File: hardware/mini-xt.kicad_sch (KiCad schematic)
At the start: 0 parts

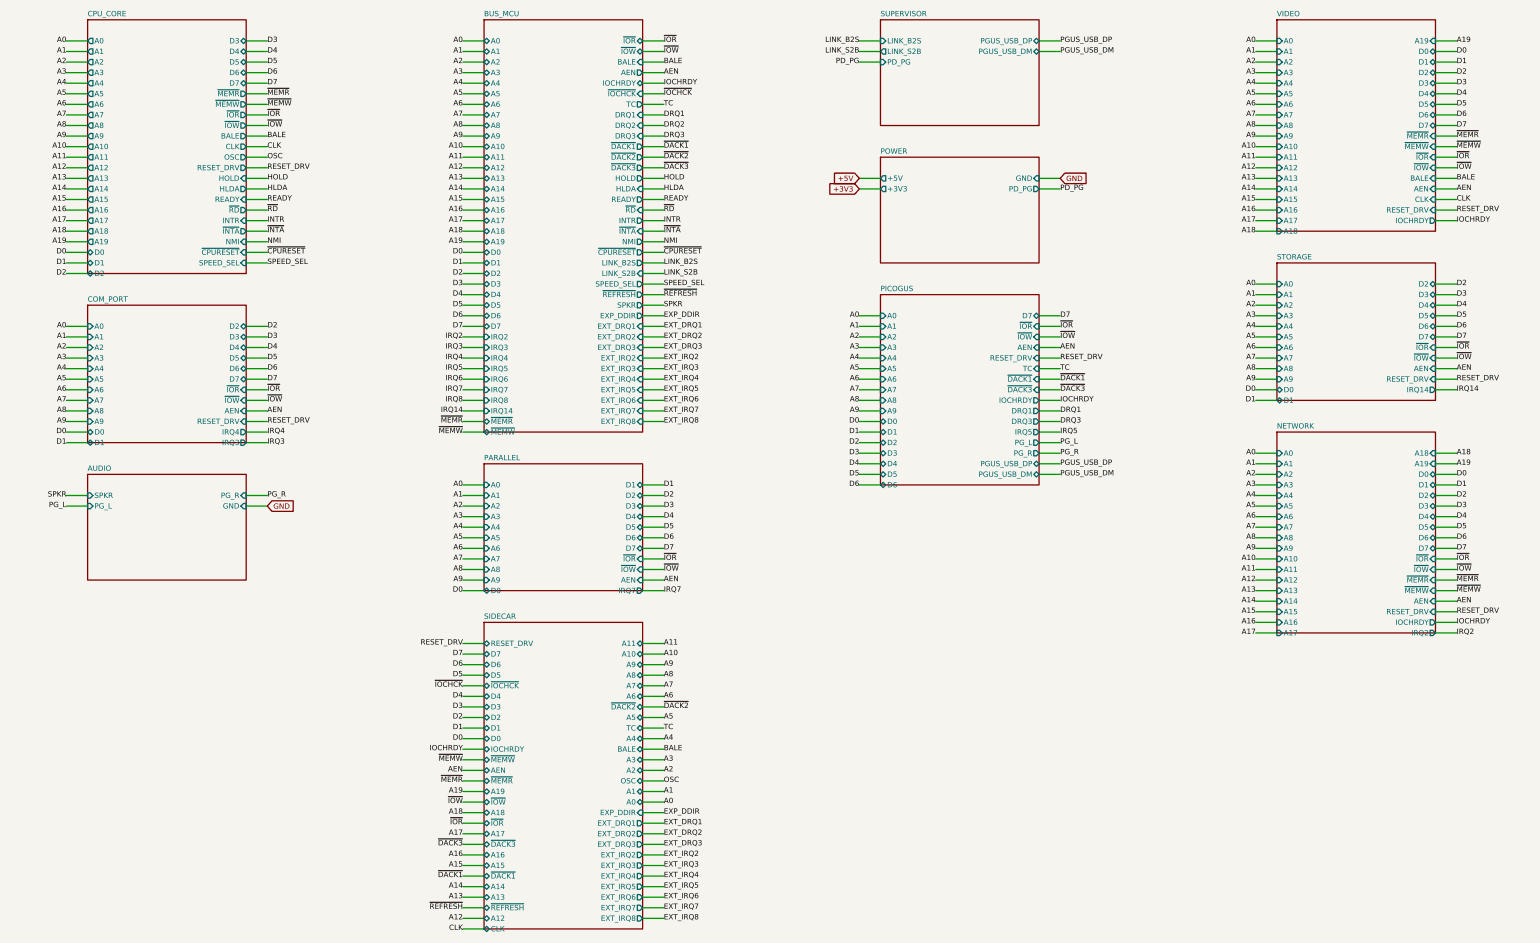
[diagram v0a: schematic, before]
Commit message: addr_decode: central I/O decode, IRQ mapping + disable jumpers; UART -> TL16C550CPFBR
New addr_decode sheet owns the discrete peripherals' bus plumbing:
'138+'00+'32 windowed decode exports ~COM1/~COM2/~LPT/~IDE chip selects
(0x3F8/0x2F8/0x378 share one A5.A4.A3 fine term); one shared 74LVC125A
maps the peripherals' private IRQ requests onto IRQ4/3/7/14 (COM keeps
~OUT2 gating), replacing the three per-sheet '125s; base straps (JP1/JP2,
pulled-high commons) and per-peripheral disable jumpers JP3-JP6 (enabled
by default, fit to disable via a second '32 rank on the CS) live here.
com_port/parallel/storage lose their decode gates, IRQ drivers and
enable jumpers; board drops 97 -> 93 ICs. Docs reframed per feedback:
PRIV_CS/PRIV_IRQREQ are shared logic factored out, not isolation breaks.

UART rebound to the active TL16C550CPFBR (TQFP-48, LCSC C882798, thin
stock) -- pinout verified identical to the symbol via jlc_get_pinout;
parts.py-only swap, sourcing notes updated.

Co-Authored-By: Claude Fable 5 <noreply@anthropic.com>
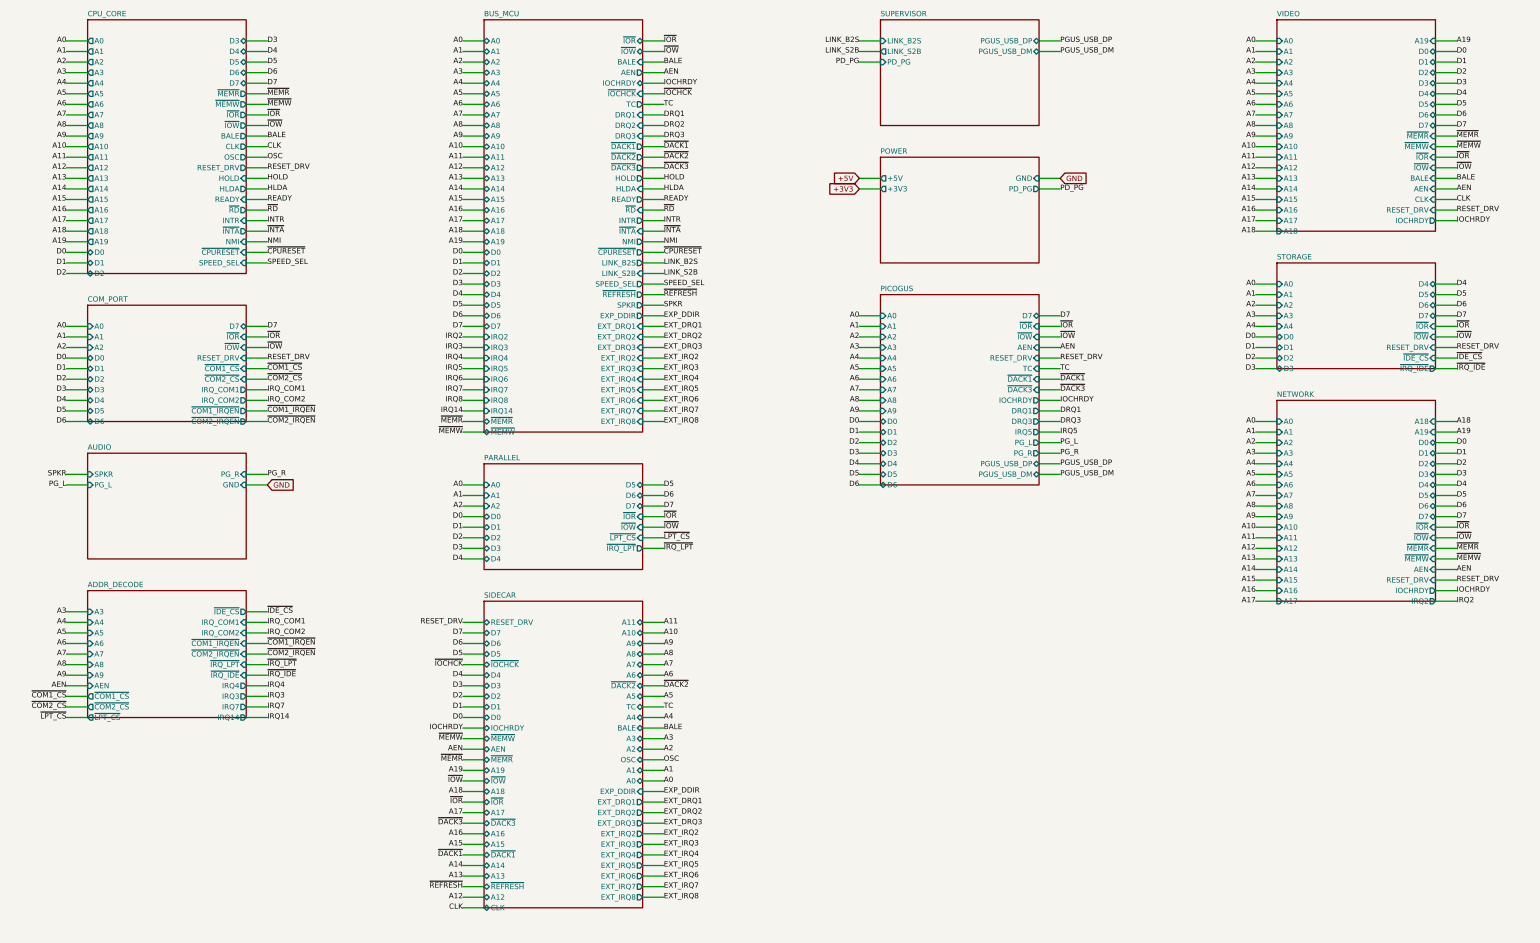
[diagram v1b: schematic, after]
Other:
- added sheet ADDR_DECODE (sheets/addr_decode.kicad_sch)
- sheet COM_PORT ports: added IRQ_COM1, IRQ_COM2, ~{COM1_CS}, ~{COM1_IRQEN}, ~{COM2_CS}, ~{COM2_IRQEN}; removed A3, A4, A5, A6, A7, A8, A9, AEN, IRQ3, IRQ4
- sheet PARALLEL ports: added ~{IRQ_LPT}, ~{LPT_CS}; removed A3, A4, A5, A6, A7, A8, A9, AEN, IRQ7
- sheet STORAGE ports: added ~{IDE_CS}, ~{IRQ_IDE}; removed A5, A6, A7, A8, A9, AEN, IRQ14

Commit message: addr_decode: hardwire LPT/IDE bases; centralize NIC + video disables (JP1-JP6)
LPT fixed at 0x378, IDE at 0x300 -- both base straps and their pull-ups
deleted ('138 ~Y1 now NC, the '00's ~A5 gate spare, IDE OR-leg takes raw
A5). The NIC and video disable jumpers move to addr_decode as JP5/JP6
with the same fit-to-disable sense as the rest: their gating hardware
stays local (the NIC's isolation '125 inside the 5V island, video's
firmware boot strap on GPIO42), only the jumper levels cross as
mxbus.PRIV_DIS -- video's documented firmware polarity inverts (high =
disabled; no firmware exists yet). Disable row is now a uniform JP1-JP6
(COM1/COM2/LPT/IDE/NIC/VID), bare board runs everything; network JP1/R6
and video JP1/R30 deleted, VID_BASE becomes video JP1. card_video's
wrapper re-adds a local DIS_VID strap (the documented PRIV lift
pattern). Docs/tables/decision logs aligned.

Co-Authored-By: Claude Fable 5 <noreply@anthropic.com>
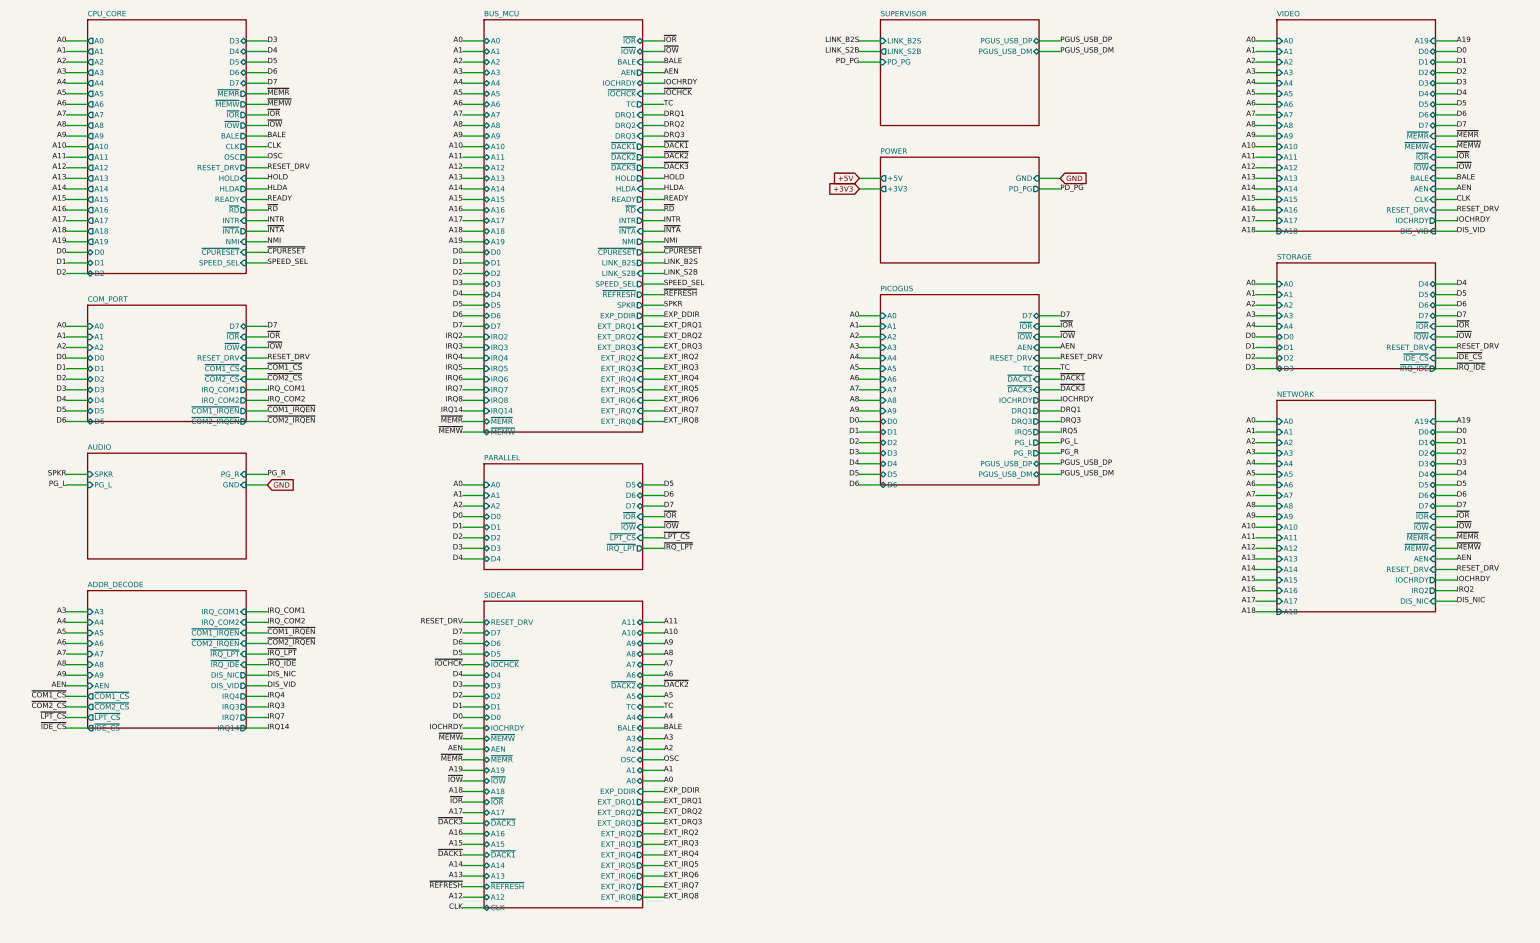
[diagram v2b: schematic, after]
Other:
- sheet ADDR_DECODE ports: added DIS_NIC, DIS_VID; removed none
- sheet NETWORK ports: added DIS_NIC; removed none
- sheet VIDEO ports: added DIS_VID; removed none

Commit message: bus_mcu: delete U17 (74LVC04A, 1/6 gates) -- HLDA inverter moves to parallel's spare gate
The HLDA -> ~{HLDA} inversion for the counter '244s now lives on the
parallel sheet's spare 74AHC14 Schmitt gate (U9.1, freed by the decode
centralization) -- the board's only spare 5V-tolerant inverter, which is
what HLDA (raw 5V V20 output) requires. ~{HLDA} joins mxbus.PRIV_CPU and
crosses as an interface net; park-safety unchanged (R18 parks HLDA low,
~{HLDA} idles high, '244s off during MCU-Hi-Z). U17 + its decoupler
deleted; the orphaned 74LVC04A parts.py line (C282341) removed. Board
454 comps / 92 ICs. Also sweeps stale JP-number refs left in the
parallel/storage/com_port docstrings from the jumper renumber.

Co-Authored-By: Claude Fable 5 <noreply@anthropic.com>
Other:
- sheet BUS_MCU ports: added ~{HLDA}; removed none
- sheet PARALLEL ports: added HLDA, ~{HLDA}; removed none

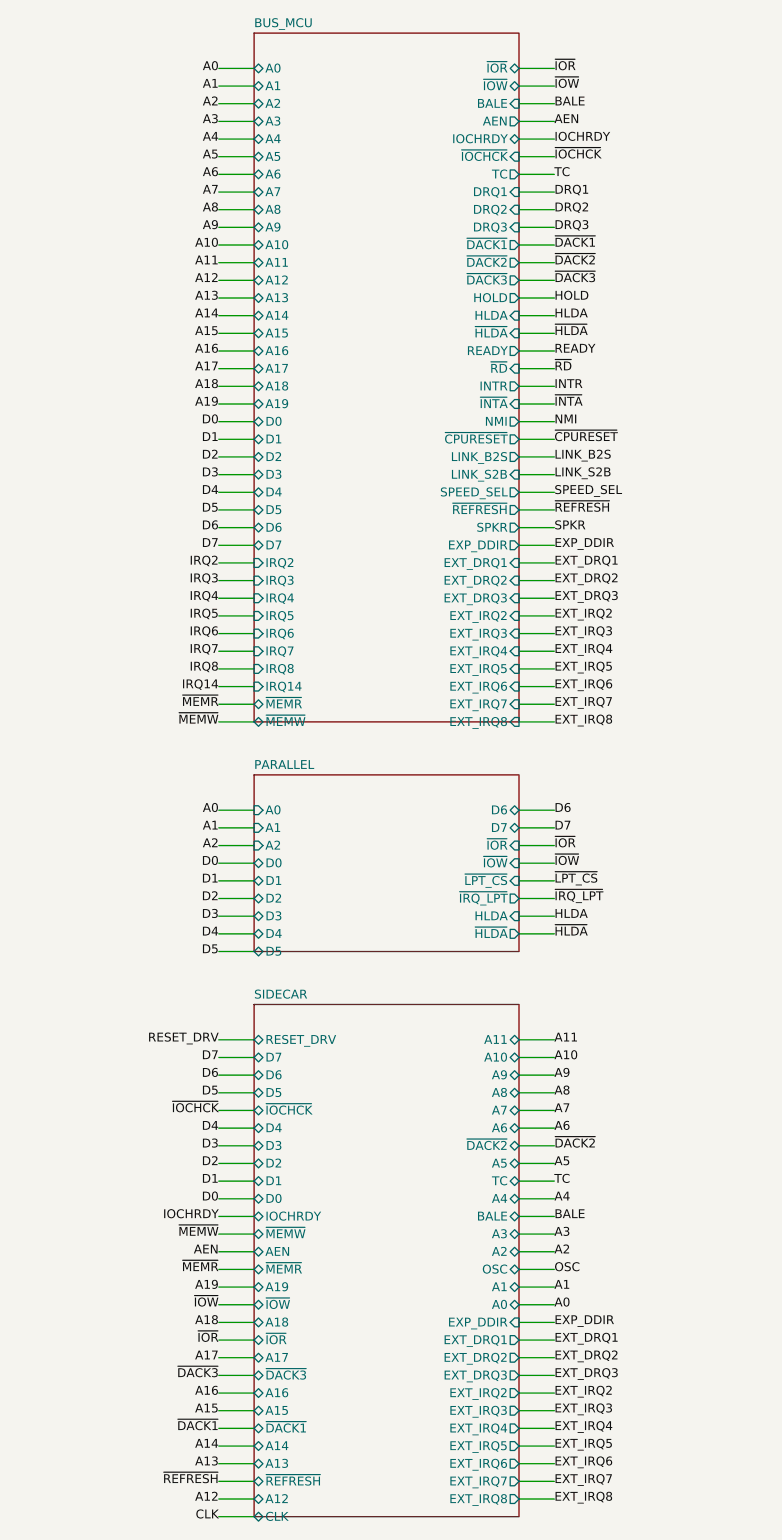
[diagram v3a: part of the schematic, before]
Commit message: ERC to zero: PWR_FLAG on VDD_RTC; retire IRQ6/IRQ8/EXT_IRQ8
Full-project ERC is now 0 errors / 0 warnings, and CLAUDE.md makes that
the standing bar. Two fixes:

- supervisor: PWR_FLAG on VDD_RTC (fed only through the D1/D2 diode-OR,
  so ERC saw no power source driving the PCF8563's VDD).
- IRQ6/IRQ8/EXT_IRQ8 formally retired (resolving the flagged IRQ8
  follow-up): none could ever be driven -- IRQ6 is a firmware floppy
  event (sidecar FDC arrives as EXT_IRQ6), IRQ8's RTC is firmware-
  emulated, EXT_IRQ8 has no header pin. Their '165 lanes tie LOW at the
  same bit positions (firmware scan map unchanged); PRIV_EXP ends at
  EXT_IRQ7; bus_mcu pulls repack 8 -> 7 full arrays. Board 405 comps /
  91 ICs. Docs + notes aligned.

Co-Authored-By: Claude Fable 5 <noreply@anthropic.com>
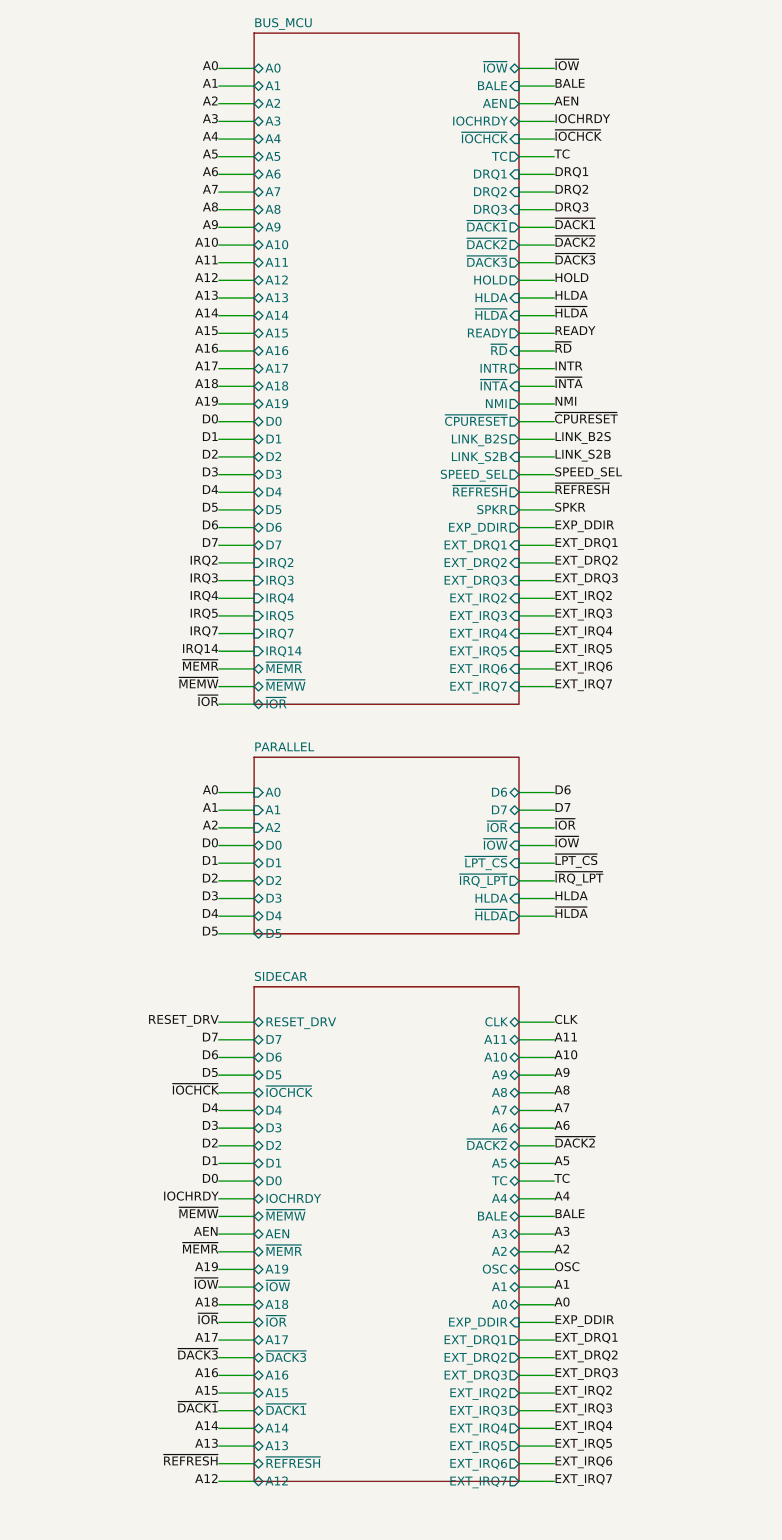
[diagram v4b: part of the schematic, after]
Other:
- sheet BUS_MCU ports: added none; removed EXT_IRQ8, IRQ6, IRQ8
- sheet SIDECAR ports: added none; removed EXT_IRQ8
